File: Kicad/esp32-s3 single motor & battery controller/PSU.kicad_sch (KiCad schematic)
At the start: 70 parts, among them J5 Batt Balance connector, Q1 NMOS,12v, Q2 NMOS, 12v, Q3 NMOS,12v, Q4 NMOS, 12v, Q5 NMOS, 12v, Q6 NMOS, 12v, U2 AP63203WU, U3 BQ76905RGRR, U4 BQ24780SRUYR

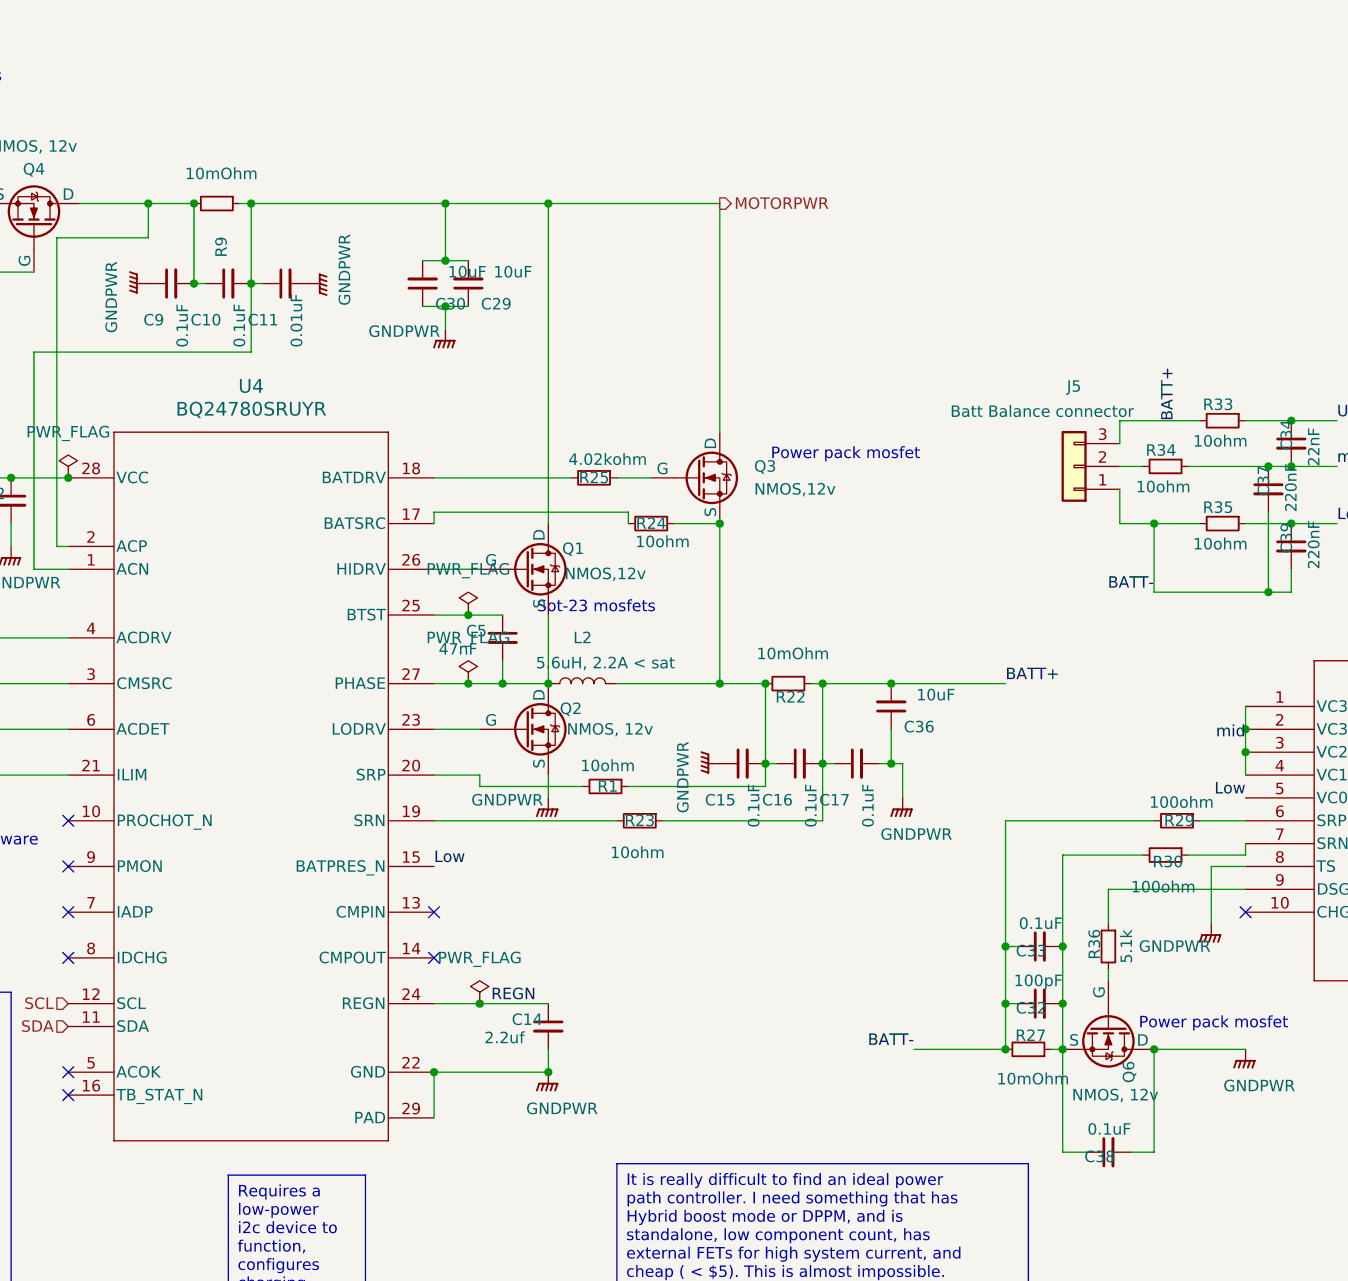
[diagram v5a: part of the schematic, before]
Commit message: Added footprints and started layout
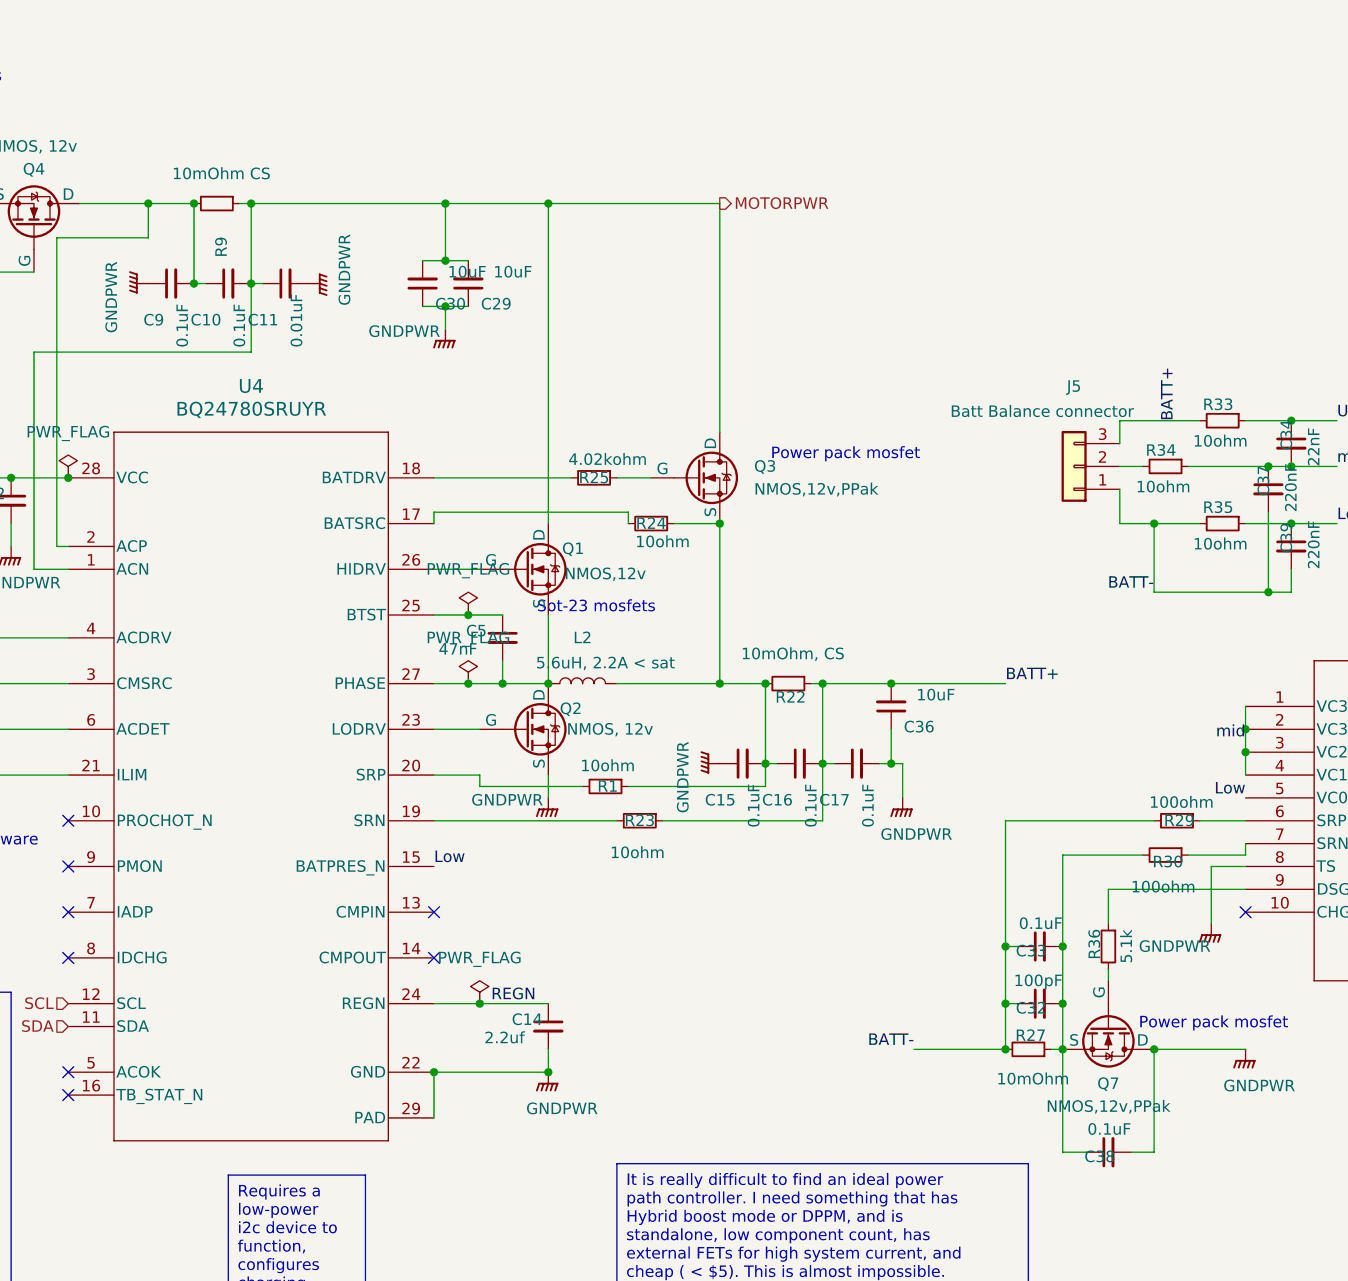
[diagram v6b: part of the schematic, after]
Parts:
- removed Q6: NMOS, 12v, symbol Simulation_SPICE:NMOS
- added Q7: NMOS,12v,PPak, Package_DFN_QFN:PQFN-8-EP_6x5mm_P1.27mm_Generic, symbol Simulation_SPICE:NMOS
- D2, D4, D5: footprint (none) -> Diode_SMD:D_0603_1608Metric
- J5: footprint (none) -> Connector_JST:JST_XH_S3B-XH-A_1x03_P2.50mm_Horizontal
- L2, L3: footprint (none) -> Inductor_SMD:L_Bourns_SDR0604
- Q1, Q2, Q4, Q5: footprint (none) -> Package_TO_SOT_SMD:SOT-323_SC-70
- Q3: value NMOS,12v -> NMOS,12v,PPak; footprint (none) -> Package_DFN_QFN:PQFN-8-EP_6x5mm_P1.27mm_Generic
- R22: value 10mOhm -> 10mOhm, CS; footprint Resistor_SMD:R_0603_1608Metric -> Resistor_SMD:R_2816_7142Metric
- R9: value 10mOhm -> 10mOhm CS; footprint Resistor_SMD:R_0603_1608Metric -> Resistor_SMD:R_2816_7142Metric
- U3: footprint VQFN20_RGR_TEX -> BQ76905:VQFN20_RGR_TEX
- U4: footprint RUY0028A -> BQ24780:RUY0028A
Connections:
- net GNDPWR: now also Q7.1 (D), Q7.2 (D), Q7.3 (D)
- net MOTORPWR: now also Q3.2 (D), Q3.3 (D)
- net at C15.2, C16.1, L2.2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: now also Q3.5 (S); no longer Q3.3 (S)
- net at C32.2, C33.2, C38.1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: now also Q7.5 (S)
- net at R25.1: now also Q3.4 (G); no longer Q3.2 (G)
- net at R36.2: now also Q7.4 (G)
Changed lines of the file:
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@@
 			)
 		)
-		(property "Footprint" ""
+		(property "Footprint" "Diode_SMD:D_0603_1608Metric"
 			(at 245.11 130.81 0)
 			(effects
@@
 			)
 		)
-		(property "Footprint" ""
+		(property "Footprint" "Package_TO_SOT_SMD:SOT-323_SC-70"
 			(at 52.07 62.23 0)
 			(effects
@@
 			)
 		)
-		(property "Footprint" ""
+		(property "Footprint" "Inductor_SMD:L_Bourns_SDR0604"
 			(at 283.21 62.23 0)
 			(effects
@@
 			)
 		)
-		(property "Footprint" ""
+		(property "Footprint" "Diode_SMD:D_0603_1608Metric"
 			(at 33.02 106.68 0)
 			(effects
@@
 			)
 		)
-		(property "Value" "10mOhm"
+		(property "Value" "10mOhm CS"
 			(at 70.358 61.468 90)
 			(effects
@@
 			)
 		)
-		(property "Footprint" "Resistor_SMD:R_0603_1608Metric"
+		(property "Footprint" "Resistor_SMD:R_2816_7142Metric"
 			(at 69.85 64.77 0)
 			(effects
@@
 			)
 		)
-		(property "Footprint" ""
+		(property "Footprint" "Connector_JST:JST_XH_S3B-XH-A_1x03_P2.50mm_Horizontal"
 			(at 165.1 93.98 0)
 			(effects
@@
 			)
 		)
-		(property "Value" "10mOhm"
+		(property "Value" "10mOhm, CS"
 			(at 133.858 114.808 90)
 			(effects
@@
 			)
 		)
-		(property "Footprint" "Resistor_SMD:R_0603_1608Metric"
+		(property "Footprint" "Resistor_SMD:R_2816_7142Metric"
 			(at 133.35 118.11 0)
 			(effects
@@
 	)
 	(symbol
+		(lib_name "NMOS_1")
+		(lib_id "Simulation_SPICE:NMOS")
+		(at 168.91 156.21 270)
+		(unit 1)
+		(exclude_from_sim no)
+		(in_bom yes)
+		(on_board yes)
+		(dnp no)
+		(fields_autoplaced yes)
+		(property "Reference" "Q7"
+			(at 168.91 162.56 90)
+			(effects
+				(font
+					(size 1.27 1.27)
+				)
+			)
+		)
+		(property "Value" "NMOS,12v,PPak"
+			(at 168.91 165.1 90)
+			(effects
+				(font
+					(size 1.27 1.27)
+				)
+			)
+		)
+		(property "Footprint" "Package_DFN_QFN:PQFN-8-EP_6x5mm_P1.27mm_Generic"
+			(at 171.45 161.29 0)
+			(effects
+				(font
+					(size 1.27 1.27)
+				)
+				(hide yes)
+			)
+		)
+		(property "Datasheet" "https://ngspice.sourceforge.io/docs/ngspice-html-manual/manual.xhtml#cha_MOSFETs"
+			(at 156.21 156.21 0)
+			(effects
+				(font
+					(size 1.27 1.27)
+				)
+				(hide yes)
+			)
+		)
+		(property "Description" "N-MOSFET transistor, drain/source/gate"
+			(at 168.91 156.21 0)
+			(effects
+				(font
+					(size 1.27 1.27)
+				)
+				(hide yes)
+			)
+		)
+		(property "Sim.Device" "NMOS"
+			(at 151.765 156.21 0)
+			(effects
+				(font
+					(size 1.27 1.27)
+				)
+				(hide yes)
+			)
+		)
+		(property "Sim.Type" "VDMOS"
+			(at 149.86 156.21 0)
+			(effects
+				(font
+					(size 1.27 1.27)
+				)
+				(hide yes)
+			)
+		)
+		(property "Sim.Pins" "1=D 2=G 3=S"
+			(at 153.67 156.21 0)
+			(effects
+				(font
+					(size 1.27 1.27)
+				)
+				(hide yes)
+			)
+		)
+		(pin "1"
+		)
+		(pin "4"
+		)
+		(pin "5"
+		)
+		(pin "2"
+		)
+		(pin "3"
+		)
+		(instances
+			(project "esp32-s3 single motor & battery controller"
+				(path "/eb3f183d-8bb1-43a5-a363-092ed67891e3/a57a0b4f-e246-497c-8d94-688647d8fd03"
+					(reference "Q7")
+					(unit 1)
+				)
+			)
+		)
+	)
+	(symbol
 		(lib_id "Device:R_Small")
 		(at 31.75 86.36 180)
@@
 			)
 		)
-		(property "Footprint" "RUY0028A"
+		(property "Footprint" "BQ24780:RUY0028A"
 			(at 73.66 128.27 0)
 			(effects
@@
 			)
 		)
-		(property "Footprint" ""
+		(property "Footprint" "Inductor_SMD:L_Bourns_SDR0604"
 			(at 110.49 118.11 0)
 			(effects
@@
 			)
 		)
-		(property "Footprint" ""
+		(property "Footprint" "Package_TO_SOT_SMD:SOT-323_SC-70"
 			(at 109.22 120.65 0)
 			(effects
@@
 	)
 	(symbol
+		(lib_name "NMOS_1")
 		(lib_id "Simulation_SPICE:NMOS")
 		(at 123.19 95.25 0)
@@
 			)
 		)
-		(property "Value" "NMOS,12v"
+		(property "Value" "NMOS,12v,PPak"
 			(at 129.54 96.5199 0)
 			(effects
@@
 			)
 		)
-		(property "Footprint" ""
+		(property "Footprint" "Package_DFN_QFN:PQFN-8-EP_6x5mm_P1.27mm_Generic"
 			(at 128.27 92.71 0)
 			(effects
@@
 			)
 		)
-		(pin "3"
-		)
 		(pin "1"
 		)
+		(pin "4"
+		)
+		(pin "5"
+		)
 		(pin "2"
 		)
+		(pin "3"
+		)
 		(instances
 			(project "esp32-s3 single motor & battery controller"
@@
 			)
 		)
-		(property "Footprint" ""
+		(property "Footprint" "Package_TO_SOT_SMD:SOT-323_SC-70"
 			(at 29.21 62.23 0)
 			(effects
@@
 			)
 		)
-		(property "Footprint" "VQFN20_RGR_TEX"
+		(property "Footprint" "BQ76905:VQFN20_RGR_TEX"
 			(at 184.15 120.65 0)
 			(effects
@@
 			)
 		)
-		(property "Footprint" ""
+		(property "Footprint" "Diode_SMD:D_0603_1608Metric"
 			(at 26.67 93.98 0)
 			(effects
@@
 	)
 	(symbol
-		(lib_id "Simulation_SPICE:NMOS")
-		(at 168.91 156.21 270)
-		(unit 1)
-		(exclude_from_sim no)
-		(in_bom yes)
-		(on_board yes)
-		(dnp no)
-		(property "Reference" "Q6"
-			(at 171.196 160.02 0)
-			(effects
-				(font
-					(size 1.27 1.27)
-				)
-				(justify left)
-			)
-		)
-		(property "Value" "NMOS, 12v"
-			(at 164.846 163.83 90)
-			(effects
-				(font
-					(size 1.27 1.27)
-				)
-				(justify left)
-			)
-		)
-		(property "Footprint" ""
-			(at 171.45 161.29 0)
-			(effects
-				(font
-					(size 1.27 1.27)
-				)
-				(hide yes)
-			)
-		)
-		(property "Datasheet" "https://ngspice.sourceforge.io/docs/ngspice-html-manual/manual.xhtml#cha_MOSFETs"
-			(at 156.21 156.21 0)
-			(effects
-				(font
-					(size 1.27 1.27)
-				)
-				(hide yes)
-			)
-		)
-		(property "Description" "N-MOSFET transistor, drain/source/gate"
-			(at 168.91 156.21 0)
-			(effects
-				(font
-					(size 1.27 1.27)
-				)
-				(hide yes)
-			)
-		)
-		(property "Sim.Device" "NMOS"
-			(at 151.765 156.21 0)
-			(effects
-				(font
-					(size 1.27 1.27)
-				)
-				(hide yes)
-			)
-		)
-		(property "Sim.Type" "VDMOS"
-			(at 149.86 156.21 0)
-			(effects
-				(font
-					(size 1.27 1.27)
-				)
-				(hide yes)
-			)
-		)
-		(property "Sim.Pins" "1=D 2=G 3=S"
-			(at 153.67 156.21 0)
-			(effects
-				(font
-					(size 1.27 1.27)
-				)
-				(hide yes)
-			)
-		)
-		(pin "3"
-		)
-		(pin "1"
-		)
-		(pin "2"
-		)
-		(instances
-			(project "esp32-s3 single motor & battery controller"
-				(path "/eb3f183d-8bb1-43a5-a363-092ed67891e3/a57a0b4f-e246-497c-8d94-688647d8fd03"
-					(reference "Q6")
-					(unit 1)
-				)
-			)
-		)
-	)
-	(symbol
 		(lib_id "Device:C_Small")
 		(at 292.1 64.77 0)
@@
 			)
 		)
-		(property "Footprint" ""
+		(property "Footprint" "Package_TO_SOT_SMD:SOT-323_SC-70"
 			(at 109.22 102.87 0)
 			(effects

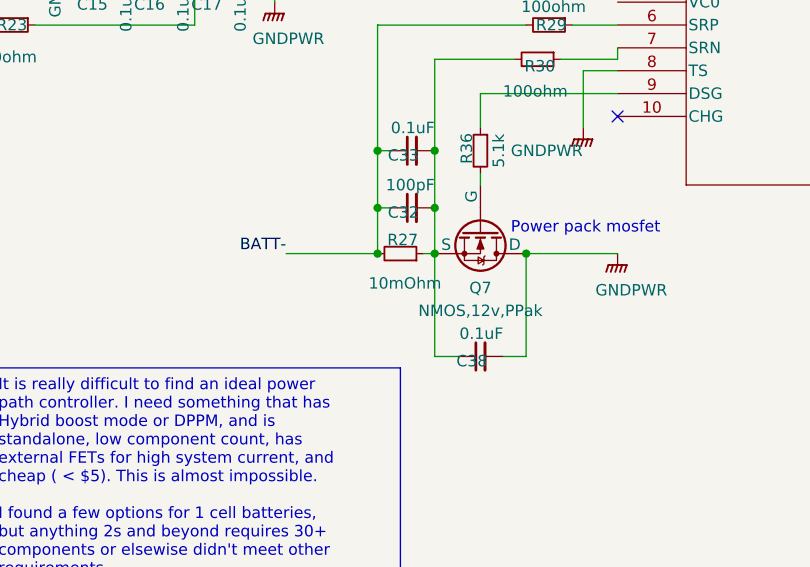
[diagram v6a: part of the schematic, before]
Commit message: Basic component layout complete
This will still change as I start wiring and switch out parts, but the basic layout is complete. 20x65mm, but my goal is 15x45mm for the size.
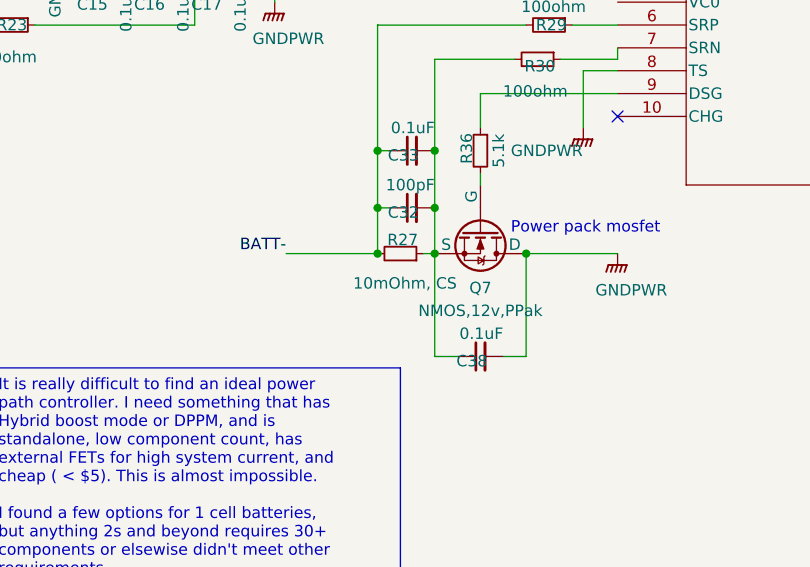
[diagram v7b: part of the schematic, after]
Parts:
- L3: footprint Inductor_SMD:L_Bourns_SDR0604 -> Inductor_SMD:L_1008_2520Metric
- R27: value 10mOhm -> 10mOhm, CS; footprint Resistor_SMD:R_0603_1608Metric -> Resistor_SMD:R_2816_7142Metric
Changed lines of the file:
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@@
 			)
 		)
-		(property "Footprint" "Inductor_SMD:L_Bourns_SDR0604"
+		(property "Footprint" "Inductor_SMD:L_1008_2520Metric"
 			(at 283.21 62.23 0)
 			(effects
@@
 			)
 		)
-		(property "Value" "10mOhm"
+		(property "Value" "10mOhm, CS"
 			(at 160.528 162.052 90)
 			(effects
@@
 			)
 		)
-		(property "Footprint" "Resistor_SMD:R_0603_1608Metric"
+		(property "Footprint" "Resistor_SMD:R_2816_7142Metric"
 			(at 160.02 158.75 0)
 			(effects

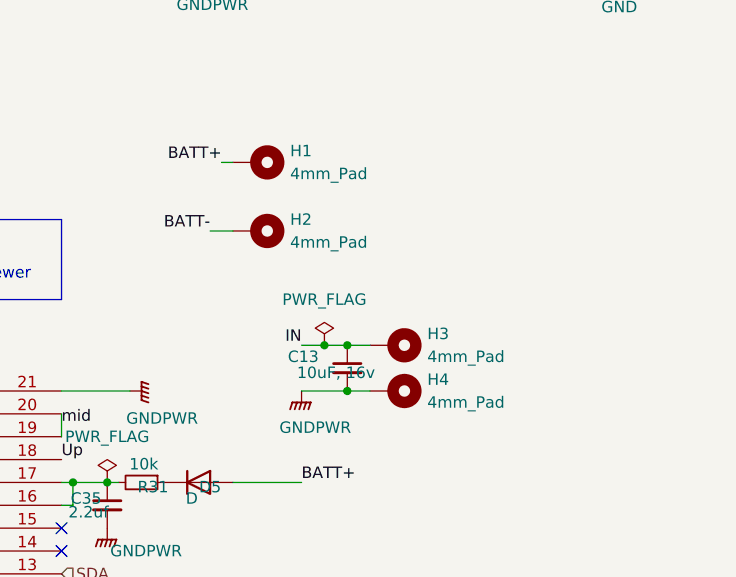
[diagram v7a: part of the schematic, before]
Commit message: Reached target dimensions of 15x45mm
I imagine heat will be crazy, but hey, its small!
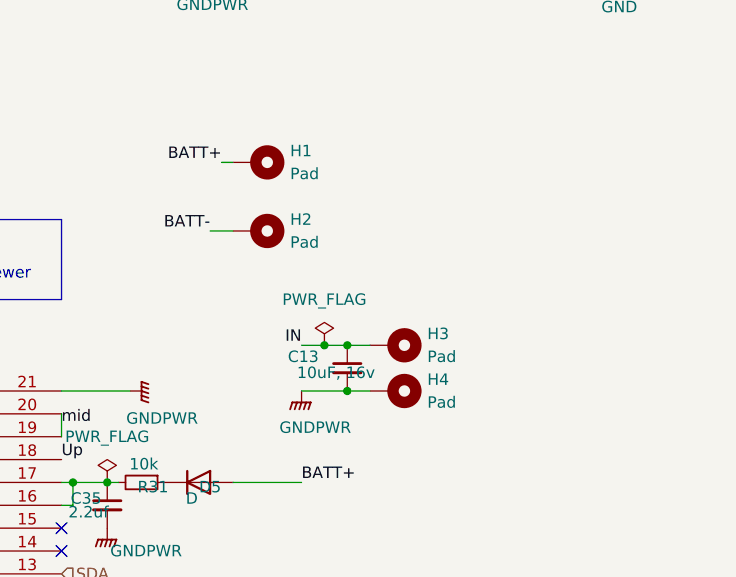
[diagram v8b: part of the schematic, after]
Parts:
- H1, H2, H3, H4: value 4mm_Pad -> Pad; footprint TestPoint:TestPoint_Pad_4.0x4.0mm -> TestPoint:TestPoint_Pad_3.0x3.0mm
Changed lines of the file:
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@@
 			)
 		)
-		(property "Value" "4mm_Pad"
+		(property "Value" "Pad"
 			(at 270.51 121.9199 90)
 			(effects
@@
 			)
 		)
-		(property "Footprint" "TestPoint:TestPoint_Pad_4.0x4.0mm"
+		(property "Footprint" "TestPoint:TestPoint_Pad_3.0x3.0mm"
 			(at 266.7 120.65 0)
 			(effects
@@
 			)
 		)
-		(property "Value" "4mm_Pad"
+		(property "Value" "Pad"
 			(at 255.27 96.5199 90)
 			(effects
@@
 			)
 		)
-		(property "Footprint" "TestPoint:TestPoint_Pad_4.0x4.0mm"
+		(property "Footprint" "TestPoint:TestPoint_Pad_3.0x3.0mm"
 			(at 251.46 95.25 0)
 			(effects
@@
 			)
 		)
-		(property "Value" "4mm_Pad"
+		(property "Value" "Pad"
 			(at 255.27 104.1399 90)
 			(effects
@@
 			)
 		)
-		(property "Footprint" "TestPoint:TestPoint_Pad_4.0x4.0mm"
+		(property "Footprint" "TestPoint:TestPoint_Pad_3.0x3.0mm"
 			(at 251.46 102.87 0)
 			(effects
@@
 			)
 		)
-		(property "Value" "4mm_Pad"
+		(property "Value" "Pad"
 			(at 270.51 116.8399 90)
 			(effects
@@
 			)
 		)
-		(property "Footprint" "TestPoint:TestPoint_Pad_4.0x4.0mm"
+		(property "Footprint" "TestPoint:TestPoint_Pad_3.0x3.0mm"
 			(at 266.7 115.57 0)
 			(effects
